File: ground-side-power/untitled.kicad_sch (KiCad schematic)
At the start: 28 parts

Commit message: Addressed comments
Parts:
- removed C? (x3): 0.1u, Capacitor_SMD:C_0805_2012Metric_Pad1.15x1.40mm_HandSolder, symbol Device:C
- removed R?: 0.0016, Resistor_SMD:R_1206_3216Metric_Pad1.42x1.75mm_HandSolder, symbol Device:R
- removed R?: 0.01, Resistor_SMD:R_1206_3216Metric_Pad1.42x1.75mm_HandSolder, symbol Device:R
- removed U? (x3): INA180, Package_TO_SOT_SMD:SOT-23-5_HandSoldering, symbol canhw:INA180
- added C10, C11, C12: 0.1u, Capacitor_SMD:C_0805_2012Metric_Pad1.15x1.40mm_HandSolder, symbol Device:C
- added F5, F6, F7, F8: Fuse, symbol Device:Fuse
- added J12, J16, J20: Extra M12, symbol Connector:Screw_Terminal_01x04
- added R14: 0.0016, Resistor_SMD:R_1206_3216Metric_Pad1.42x1.75mm_HandSolder, symbol Device:R
- added R15: 0.01, Resistor_SMD:R_1206_3216Metric_Pad1.42x1.75mm_HandSolder, symbol Device:R
- added U4, U5, U6: INA180, Package_TO_SOT_SMD:SOT-23-5_HandSoldering, symbol canhw:INA180
- R10: renamed from R?; value 1.5k -> 2.2K
- R11, R7: renamed from R?; value R -> 1K
- R12: renamed from R?; value R -> 6.6K
- R5: renamed from R?; value R -> 1k
- R6: renamed from R?; value R -> 2.2K
- R8: renamed from R?; value R -> 330
- gave numbers to parts that had none: 13
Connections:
- net CURR_12V is gone; now on net +12V: R9.1
- net CURR_5V is gone; now on net +5V: R7.1
- net +12V: now also R16.1, R5.1, U3.4 (IN-), J12.2 (Pin_2), J16.2 (Pin_2), J20.2 (Pin_2), R14.2, R15.2, U4.4 (IN-), U5.4 (IN-), U6.4 (IN-); no longer U3.3 (IN+)
- net +24V: now also R11.1, J12.1 (Pin_1), J16.1 (Pin_1), J20.1 (Pin_1); no longer R16.2
- net +5V: now also C10.2, C11.2, C12.2, J12.3 (Pin_3), J16.3 (Pin_3), J20.3 (Pin_3), U4.5 (VS), U5.5 (VS), U6.5 (VS)
- net 12V_OUT: now also U4.1 (VO)
- net 24V_OUT: now also U6.1 (VO)
- net 5V_OUT: now also U5.1 (VO)
- net GND: now also C10.1, C11.1, C12.1, J12.4 (Pin_4), J16.4 (Pin_4), J20.4 (Pin_4), U4.2 (GND), U5.2 (GND), U6.2 (GND)
- removed net CURR_24V: R11.1, R16.1
- removed net CURR_DRAW: R13.1, R5.1, U3.4 (IN-)
- new net: F6.2, R14.1, U4.3 (IN+)
- new net: F7.2, R15.1, U5.3 (IN+)
- new net: F5.2, R13.1, U3.3 (IN+)
- new net: F8.2, R16.2, U6.3 (IN+)
- new net 12V_UNSENSED: F6.1
- new net 24V_UNSENSED: F8.1
- new net 5V_UNSENSED: F7.1
- new net SYSTEM_UNSENSED: F5.1
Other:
- moved on the sheet: C9, J13, J17, R10, R11, R12, R13, R16, R5, R6, R7, R8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

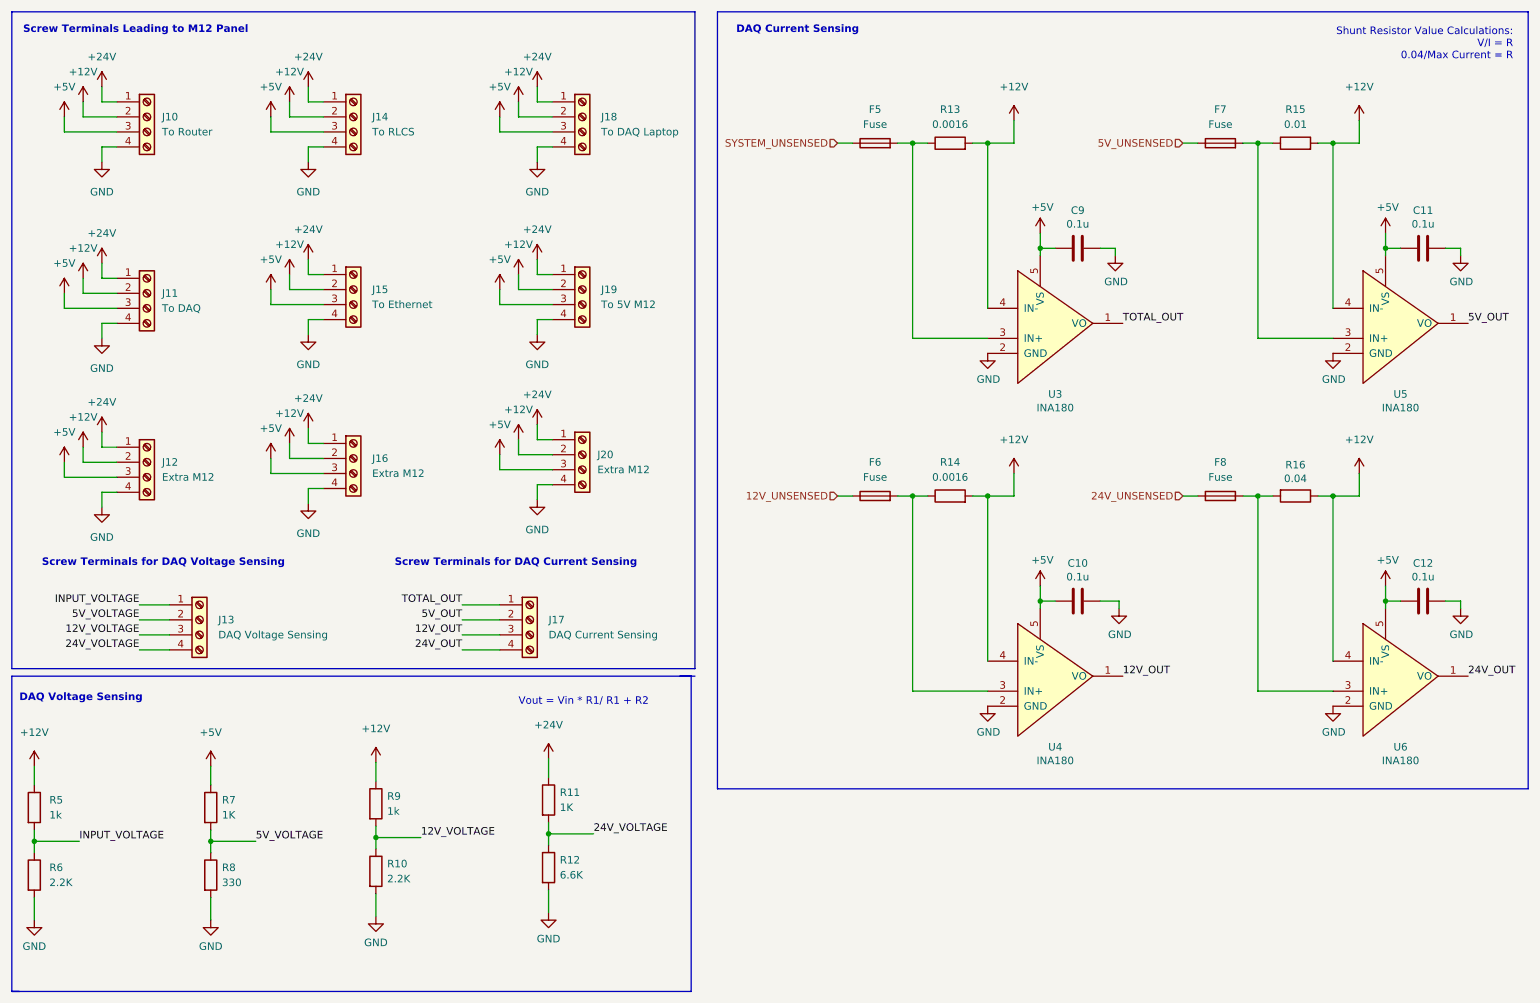
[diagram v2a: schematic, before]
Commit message: Changes to Shunt Current Sensors
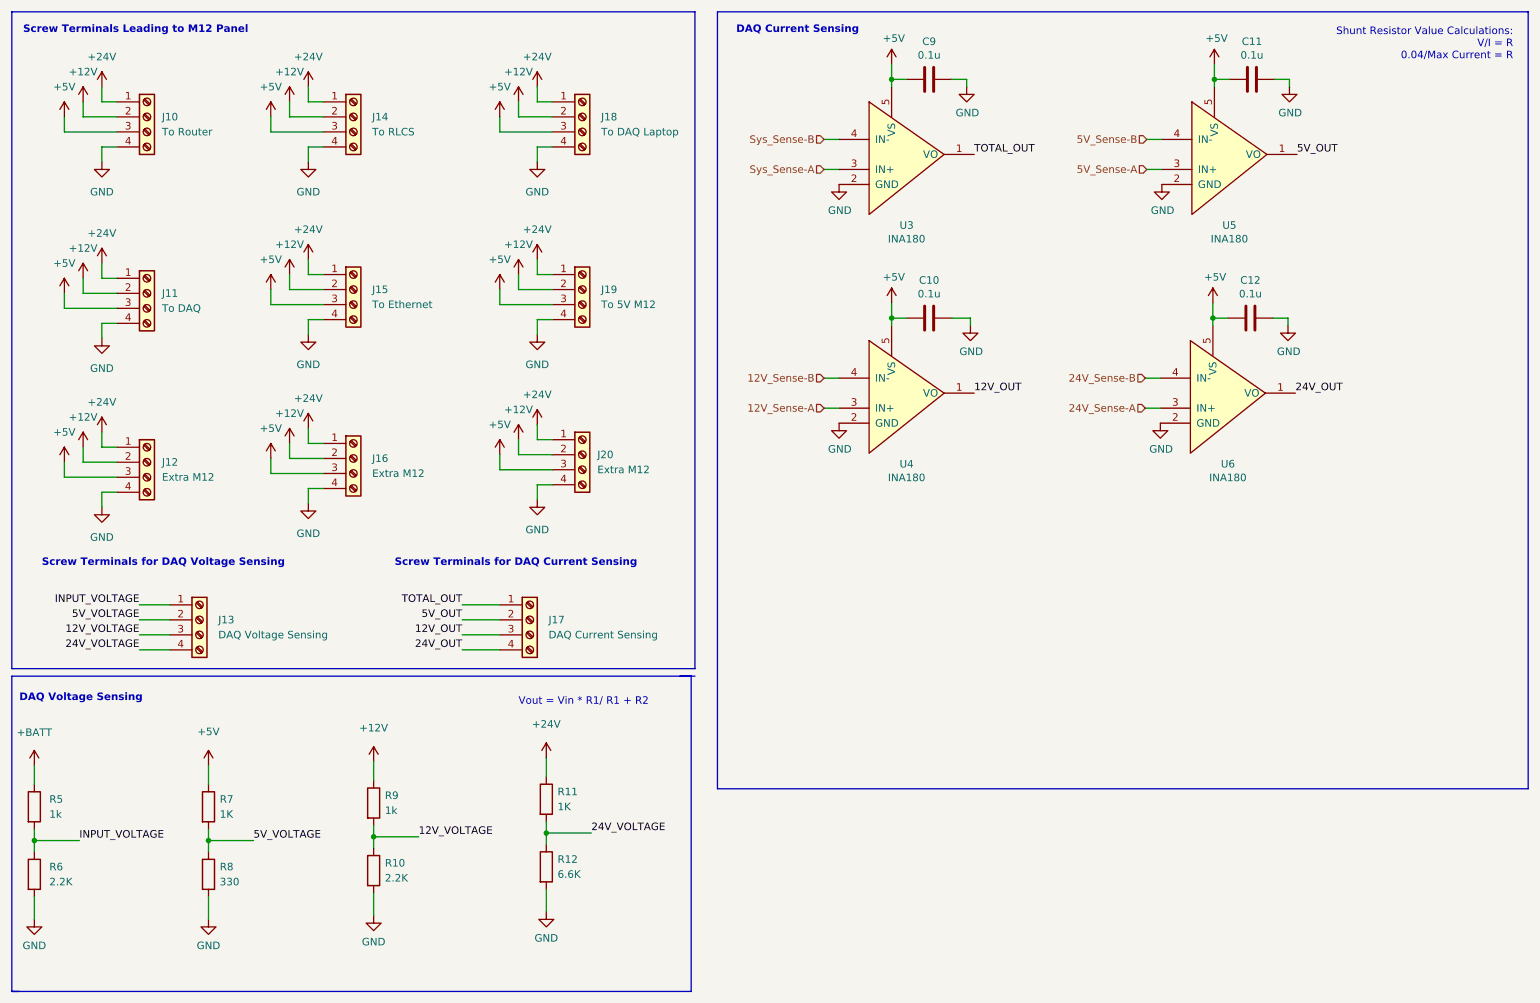
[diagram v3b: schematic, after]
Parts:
- removed F5, F6, F7, F8: Fuse, symbol Device:Fuse
- removed R13, R14: 0.0016, Resistor_SMD:R_1206_3216Metric_Pad1.42x1.75mm_HandSolder, symbol Device:R
- removed R15: 0.01, Resistor_SMD:R_1206_3216Metric_Pad1.42x1.75mm_HandSolder, symbol Device:R
- removed R16: 0.04, Resistor_SMD:R_1206_3216Metric_Pad1.42x1.75mm_HandSolder, symbol Device:R
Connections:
- net +12V: no longer R5.1, U3.4 (IN-), U4.4 (IN-), U5.4 (IN-), U6.4 (IN-)
- net 12V_Sense-A: now reaches U4.3 (IN+)
- net 5V_Sense-A: now reaches U5.3 (IN+)
- net Sys_Sense-A: now reaches U3.3 (IN+)
- net 24V_Sense-A: now reaches U6.3 (IN+)
- new net +BATT: R5.1
- new net 12V_Sense-B: U4.4 (IN-)
- new net 24V_Sense-B: U6.4 (IN-)
- new net 5V_Sense-B: U5.4 (IN-)
- new net Sys_Sense-B: U3.4 (IN-)
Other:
- moved on the sheet: C10, C11, C12, C9, U3, U4, U5, U6

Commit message: Addressed remaining comments
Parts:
- removed R5: 1k, symbol Device:R
- removed R6: 2.2K, symbol Device:R
- R10: value 2.2K -> 100K
- R11: value 1K -> 660K
- R12: value 6.6K -> 100K
- R7: value 1K -> 47K
- R8: value 330 -> 100K
- R9: value 1k -> 220K
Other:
- note added: "Vout = Vin * R2/ R1 + R2"
- note removed: "Vout = Vin * R1/ R1 + R2"
- moved on the sheet: R10, R11, R12, R7, R8, R9

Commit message: Resolved Remaining Schematic Issues
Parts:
- renumbered C9 to C11, C11 to C12, C10 to C13, C12 to C14, J18 to J10, J15 to J11, J19 to J12, J11 to J13, J20 to J14, J16 to J15, J12 to J16, J13 to J17, J17 to J18, J10 to J8, J14 to J9, R11 to R10, R7 to R11, R10 to R12, R12 to R13, R8 to R14, U5 to U4, U4 to U5
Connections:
- net 12V_Sense-A renamed 12V_Sense+
- net 12V_Sense-B renamed 12V_Sense-
- net 24V_Sense-A renamed 24V_Sense+
- net 24V_Sense-B renamed 24V_Sense-
- net 5V_Sense-A renamed 5V_Sense+
- net 5V_Sense-B renamed 5V_Sense-
- net INPUT_VOLTAGE renamed +BATT
- net Sys_Sense-A renamed Sys_Sense+
- net Sys_Sense-B renamed Sys_Sense-

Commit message: Added Footprints
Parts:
- J10, J11, J12, J13, J14, J15, J16, J17, J18, J8, J9: footprint (none) -> GSP:EB21A-04-D
- R10, R11: footprint (none) -> Resistor_SMD:R_0603_1608Metric_Pad0.98x0.95mm_HandSolder
- R12, R13, R14, R9: footprint (none) -> Resistor_SMD:R_0402_1005Metric_Pad0.72x0.64mm_HandSolder
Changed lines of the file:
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@@
       (effects (font (size 1.27 1.27)) (justify left))
     )
-    (property "Footprint" "" (id 2) (at 86.233 174.752 90)
+    (property "Footprint" "Resistor_SMD:R_0402_1005Metric_Pad0.72x0.64mm_HandSolder" (id 2) (at 86.233 174.752 90)
       (effects (font (size 1.27 1.27)) hide)
     )
@@
       (effects (font (size 1.27 1.27)) (justify left))
     )
-    (property "Footprint" "" (id 2) (at 121.92 46.99 0)
+    (property "Footprint" "GSP:EB21A-04-D" (id 2) (at 121.92 46.99 0)
       (effects (font (size 1.27 1.27)) hide)
     )
@@
       (effects (font (size 1.27 1.27)) (justify left))
     )
-    (property "Footprint" "" (id 2) (at 48.26 46.99 0)
+    (property "Footprint" "GSP:EB21A-04-D" (id 2) (at 48.26 46.99 0)
       (effects (font (size 1.27 1.27)) hide)
     )
@@
       (effects (font (size 1.27 1.27)) (justify left))
     )
-    (property "Footprint" "" (id 2) (at 48.26 76.835 0)
+    (property "Footprint" "GSP:EB21A-04-D" (id 2) (at 48.26 76.835 0)
       (effects (font (size 1.27 1.27)) hide)
     )
@@
       (effects (font (size 1.27 1.27)) (justify left))
     )
-    (property "Footprint" "" (id 2) (at 48.26 105.41 0)
+    (property "Footprint" "GSP:EB21A-04-D" (id 2) (at 48.26 105.41 0)
       (effects (font (size 1.27 1.27)) hide)
     )
@@
       (effects (font (size 1.27 1.27)) (justify left))
     )
-    (property "Footprint" "" (id 2) (at 29.337 163.83 90)
+    (property "Footprint" "Resistor_SMD:R_0603_1608Metric_Pad0.98x0.95mm_HandSolder" (id 2) (at 29.337 163.83 90)
       (effects (font (size 1.27 1.27)) hide)
     )
@@
       (effects (font (size 1.27 1.27)) (justify left))
     )
-    (property "Footprint" "" (id 2) (at 29.337 175.26 90)
+    (property "Footprint" "Resistor_SMD:R_0402_1005Metric_Pad0.72x0.64mm_HandSolder" (id 2) (at 29.337 175.26 90)
       (effects (font (size 1.27 1.27)) hide)
     )
@@
       (effects (font (size 1.27 1.27)) (justify left))
     )
-    (property "Footprint" "" (id 2) (at 113.03 132.08 0)
+    (property "Footprint" "GSP:EB21A-04-D" (id 2) (at 113.03 132.08 0)
       (effects (font (size 1.27 1.27)) hide)
     )
@@
       (effects (font (size 1.27 1.27)) (justify left))
     )
-    (property "Footprint" "" (id 2) (at 83.185 46.99 0)
+    (property "Footprint" "GSP:EB21A-04-D" (id 2) (at 83.185 46.99 0)
       (effects (font (size 1.27 1.27)) hide)
     )
@@
       (effects (font (size 1.27 1.27)) (justify left))
     )
-    (property "Footprint" "" (id 2) (at 86.233 163.322 90)
+    (property "Footprint" "Resistor_SMD:R_0603_1608Metric_Pad0.98x0.95mm_HandSolder" (id 2) (at 86.233 163.322 90)
       (effects (font (size 1.27 1.27)) hide)
     )
@@
       (effects (font (size 1.27 1.27)) (justify left))
     )
-    (property "Footprint" "" (id 2) (at 83.185 104.775 0)
+    (property "Footprint" "GSP:EB21A-04-D" (id 2) (at 83.185 104.775 0)
       (effects (font (size 1.27 1.27)) hide)
     )
@@
       (effects (font (size 1.27 1.27)) (justify left))
     )
-    (property "Footprint" "" (id 2) (at 121.92 104.14 0)
+    (property "Footprint" "GSP:EB21A-04-D" (id 2) (at 121.92 104.14 0)
       (effects (font (size 1.27 1.27)) hide)
     )
@@
       (effects (font (size 1.27 1.27)) (justify left))
     )
-    (property "Footprint" "" (id 2) (at 121.92 76.2 0)
+    (property "Footprint" "GSP:EB21A-04-D" (id 2) (at 121.92 76.2 0)
       (effects (font (size 1.27 1.27)) hide)
     )
@@
       (effects (font (size 1.27 1.27)) (justify left))
     )
-    (property "Footprint" "" (id 2) (at 57.15 132.08 0)
+    (property "Footprint" "GSP:EB21A-04-D" (id 2) (at 57.15 132.08 0)
       (effects (font (size 1.27 1.27)) hide)
     )
@@
       (effects (font (size 1.27 1.27)) (justify left))
     )
-    (property "Footprint" "" (id 2) (at 83.185 76.2 0)
+    (property "Footprint" "GSP:EB21A-04-D" (id 2) (at 83.185 76.2 0)
       (effects (font (size 1.27 1.27)) hide)
     )
@@
       (effects (font (size 1.27 1.27)) (justify left))
     )
-    (property "Footprint" "" (id 2) (at 57.277 163.195 90)
+    (property "Footprint" "Resistor_SMD:R_0402_1005Metric_Pad0.72x0.64mm_HandSolder" (id 2) (at 57.277 163.195 90)
       (effects (font (size 1.27 1.27)) hide)
     )
@@
       (effects (font (size 1.27 1.27)) (justify left))
     )
-    (property "Footprint" "" (id 2) (at 57.277 174.625 90)
-      (effects (font (size 1.27 1.27)) hide)
-    )
+    (property "Footprint" "Resistor_SMD:R_0402_1005Metric_Pad0.72x0.64mm_HandSolder" (id 2) (at 57.277 174.625 90)
+      (effects (font (size 1.27 1.27)) hide)
+    )

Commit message: Fixed footprints
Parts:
- C11, C12, C13, C14: footprint Capacitor_SMD:C_0805_2012Metric_Pad1.15x1.40mm_HandSolder -> Capacitor_SMD:C_0805_2012Metric_Pad1.18x1.45mm_HandSolder
